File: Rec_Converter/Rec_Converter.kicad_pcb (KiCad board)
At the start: 2 copper layers, 37.8 x 33 mm, 8 parts, among them J1 RJ45, J2 RJ45

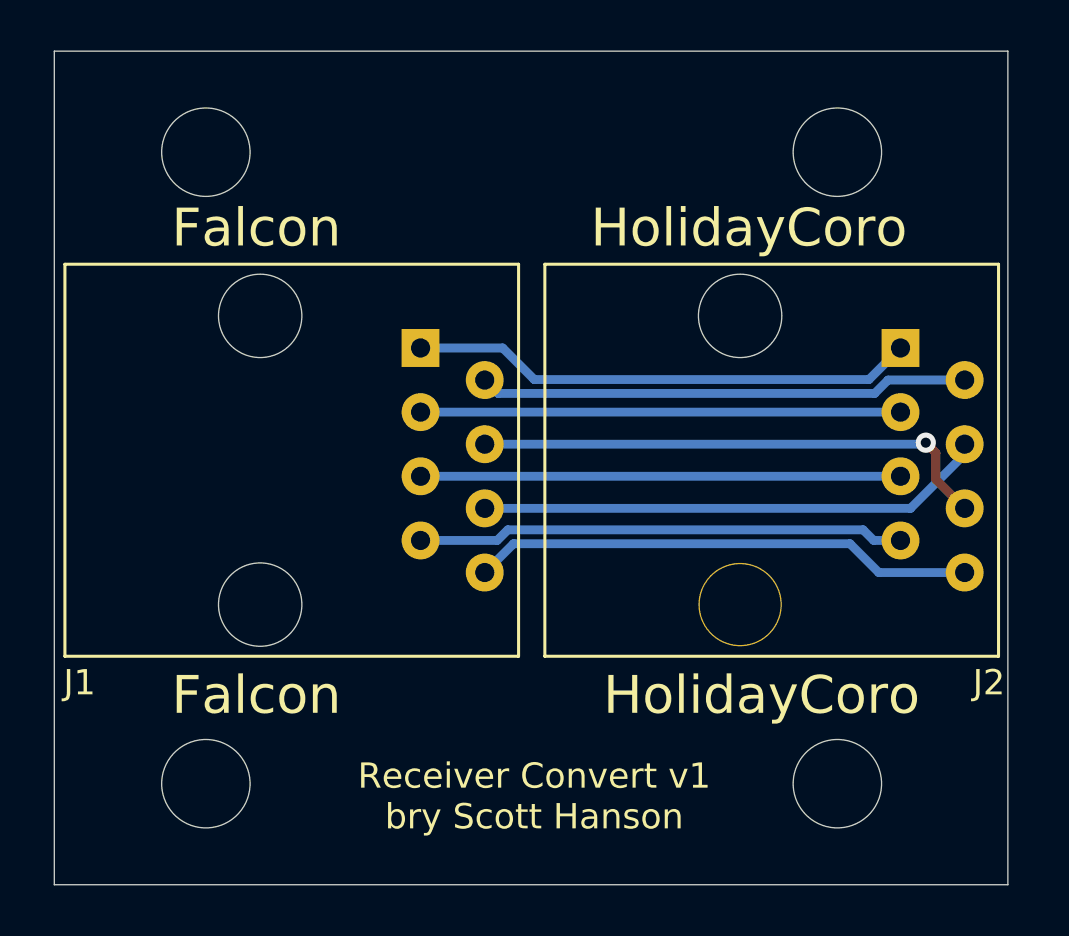
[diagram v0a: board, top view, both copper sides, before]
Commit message: rotated connectors
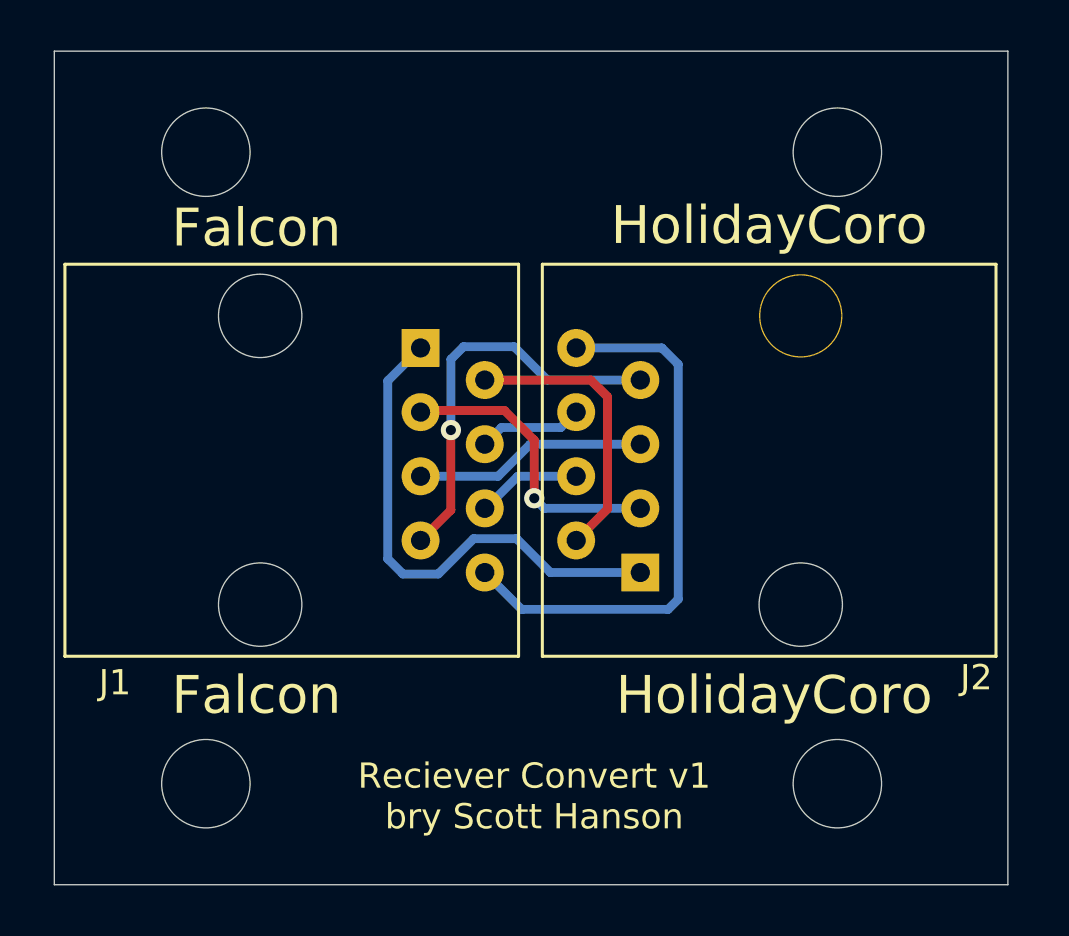
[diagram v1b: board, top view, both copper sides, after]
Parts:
- removed REF**: KiCad-Logo2_6mm_SilkScreen, Symbol:KiCad-Logo2_6mm_SilkScreen
- removed REF**: OSHW-Logo2_9.8x8mm_SilkScreen, Symbol:OSHW-Logo2_9.8x8mm_SilkScreen
- moved J2 13.6 mm to (156.2, 114.6), turned to 90 degrees
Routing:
- net Net-(J1-Pad4): track 20.7 -> 4.15 mm, vias 1 -> 0
- net Net-(J1-Pad6): track 20.3 -> 4.15 mm
- net Net-(J1-Pad5): track 19.0 -> 9.23 mm
- net Net-(J1-Pad2): track 19.4 -> 11.3 mm
- net Net-(J1-Pad3): track 19.0 -> 11.7 mm, vias 0 -> 1
- net Net-(J1-Pad7): track 19.4 -> 16.0 mm, vias 0 -> 1
- net Net-(J1-Pad8): track 19.9 -> 22.0 mm
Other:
- board text added: "Reciever Convert v1 bry Scott Hanson"
- board text removed: "Receiver Convert v1 bry Scott Hanson"

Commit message: added schematic
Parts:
- moved J1 9.87 mm to (146.9, 115.6), turned to 180 degrees
- moved J2 9.05 mm to (165.2, 115.6), turned to 180 degrees
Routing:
- net Net-(J1-Pad6): track 4.15 -> 22.3 mm
- net Net-(J1-Pad4): track 4.15 -> 16.8 mm
- net Net-(J1-Pad5): track 9.23 -> 21.2 mm, vias 0 -> 1
- net Net-(J1-Pad3): track 11.7 -> 22.1 mm
- net Net-(J1-Pad2): track 11.3 -> 19.3 mm
- net Net-(J1-Pad7): track 16.0 -> 19.4 mm, vias 1 -> 0
- net Net-(J1-Pad1): track 20.3 -> 23.2 mm, vias 0 -> 1
- net Net-(J1-Pad8): track 22.0 -> 19.4 mm, vias 0 -> 1
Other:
- board size 37.8 x 33 mm -> 34 x 33 mm
